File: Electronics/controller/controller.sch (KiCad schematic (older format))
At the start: 26 parts, among them P1 POWER, P2 PANEL_1, P3 PANEL_2, Q1 P55NF, SW1 SW_PUSH, U1 LM7805CT, U2 74HC595, U3 Arduino_Pro_Micro

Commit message: Moved some parts around on the board.
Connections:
- net D18: now also R2.1, SW1.1
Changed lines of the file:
@@
 EESchema Schematic File Version 2
-LIBS:cylindric
-LIBS:borniers
 LIBS:power
 LIBS:device
@@
 LIBS:contrib
 LIBS:valves
-LIBS:controller-cache
+LIBS:borniers
+LIBS:cylindric
+LIBS:digit_board-cache
 EELAYER 25 0
 EELAYER END
@@
 	1    0    0    -1
 $EndComp
-Text Label 7225 1300 0    60   ~ 0
+Text Label 7200 1300 0    60   ~ 0
 D18
 Text Notes 7200 750  0    60   ~ 0
@@
 	4100 2350 4100 2450
 Wire Wire Line
-	3900 2350 4300 2350
+	3900 2350 4100 2350
+Wire Wire Line
+	4100 2350 4300 2350
 Wire Wire Line
 	4500 1500 4550 1500
@@
 	4450 1700 4550 1700
 Wire Wire Line
-	4500 950  4500 1500
+	4500 950  4500 1100
+Wire Wire Line
+	4500 1100 4500 1500
 Wire Wire Line
 	4500 1100 4550 1100
@@
 	3900 2250 3900 2350
 Wire Wire Line
-	5700 1800 6600 1800
-Wire Wire Line
-	5700 1350 6250 1350
-Wire Wire Line
-	1450 1400 1850 1400
+	5700 1800 6000 1800
+Wire Wire Line
+	6000 1800 6600 1800
+Wire Wire Line
+	5700 1350 6000 1350
+Wire Wire Line
+	6000 1350 6250 1350
+Wire Wire Line
+	1450 1400 1650 1400
+Wire Wire Line
+	1650 1400 1850 1400
 Connection ~ 1650 1400
 Wire Wire Line
-	1650 1150 1650 1550
+	1650 1150 1650 1400
+Wire Wire Line
+	1650 1400 1650 1550
 Wire Wire Line
 	2250 2050 2250 1700
 Wire Wire Line
-	1450 2050 2825 2050
+	1450 2050 1650 2050
+Wire Wire Line
+	1650 2050 1800 2050
+Wire Wire Line
+	1800 2050 2250 2050
+Wire Wire Line
+	2250 2050 2825 2050
 Connection ~ 1800 2050
 Wire Notes Line
@@
 	10700 2800 8600 2800
 Wire Wire Line
-	5700 900  6600 900
+	5700 900  6000 900
+Wire Wire Line
+	6000 900  6600 900
 Wire Wire Line
 	5700 1350 5700 1400
@@
 	4300 1350 4300 1300
 Wire Wire Line
-	4300 1300 4550 1300
+	4300 1300 4450 1300
+Wire Wire Line
+	4450 1300 4550 1300
 Wire Wire Line
 	3900 1750 3900 1600
 Wire Wire Line
-	3750 1600 4000 1600
+	3750 1600 3900 1600
+Wire Wire Line
+	3900 1600 4000 1600
 Wire Wire Line
 	3200 3250 3400 3250
@@
 	1350 5350 1350 5100
 Wire Bus Line
-	3500 4525 6150 4525
+	3500 4375 6150 4375
 Entry Wire Line
 	3400 3250 3500 3350
@@
 	3400 3950 3500 4050
 Wire Bus Line
-	3500 3175 3500 4525
+	3500 3175 3500 3350
+Wire Bus Line
+	3500 3350 3500 3450
+Wire Bus Line
+	3500 3450 3500 3550
+Wire Bus Line
+	3500 3550 3500 3650
+Wire Bus Line
+	3500 3650 3500 3750
+Wire Bus Line
+	3500 3750 3500 3850
+Wire Bus Line
+	3500 3850 3500 3950
+Wire Bus Line
+	3500 3950 3500 3900
+Wire Bus Line
+	3500 3900 3500 4375
 Entry Wire Line
 	6050 4850 6150 4750
@@
 	6050 5550 6150 5450
 Wire Bus Line
-	6150 4525 6150 5600
+	6150 4375 6150 4600
+Wire Bus Line
+	6150 4600 6150 4750
+Wire Bus Line
+	6150 4750 6150 4850
+Wire Bus Line
+	6150 4850 6150 4950
+Wire Bus Line
+	6150 4950 6150 5050
+Wire Bus Line
+	6150 5050 6150 5150
+Wire Bus Line
+	6150 5150 6150 5250
+Wire Bus Line
+	6150 5250 6150 5350
+Wire Bus Line
+	6150 5350 6150 5450
+Wire Bus Line
+	6150 5450 6150 5600
 Wire Wire Line
 	9050 2050 8900 2050
@@
 $EndComp
 Wire Wire Line
-	2825 1150 2825 1550
+	2825 1150 2825 1400
+Wire Wire Line
+	2825 1400 2825 1550
 Connection ~ 2825 1400
 Wire Wire Line
@@
 $EndComp
 Wire Wire Line
-	7400 1150 7400 1450
+	7400 1150 7400 1300
+Wire Wire Line
+	7400 1300 7400 1450
 Wire Wire Line
 	7400 1450 7500 1450
@@
 $EndComp
 Wire Wire Line
-	7400 1300 7250 1300
+	7400 1300 7200 1300
 Connection ~ 7400 1300
 $EndSCHEMATC

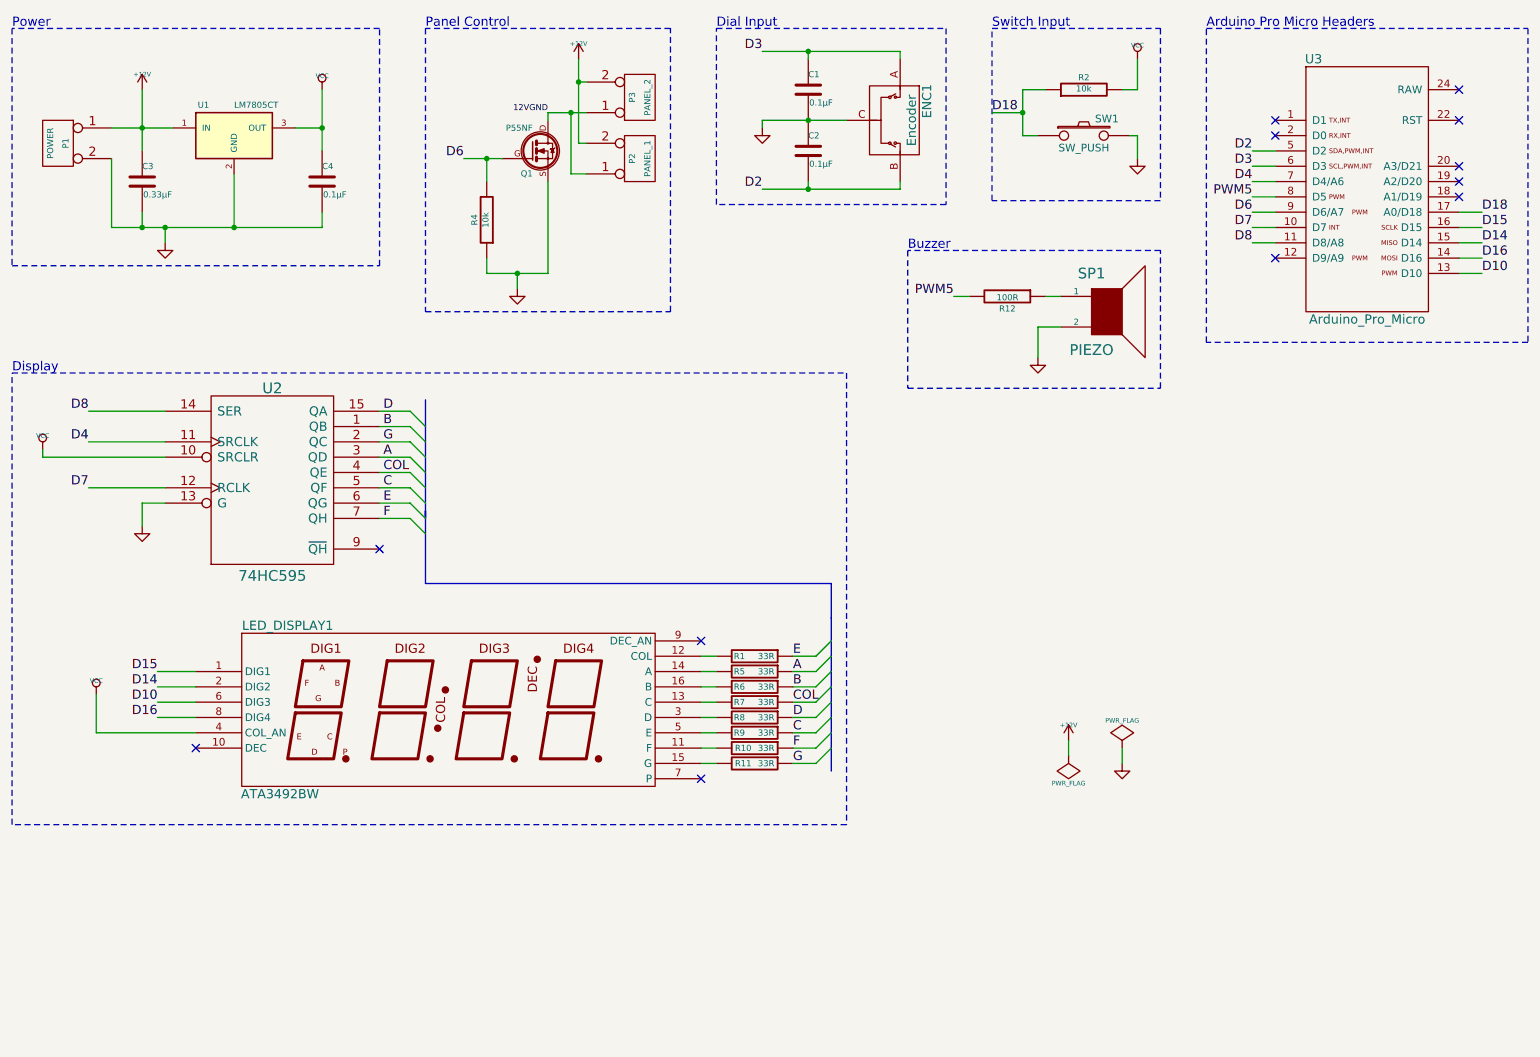
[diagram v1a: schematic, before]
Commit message: Tidied up some visual layout issues.
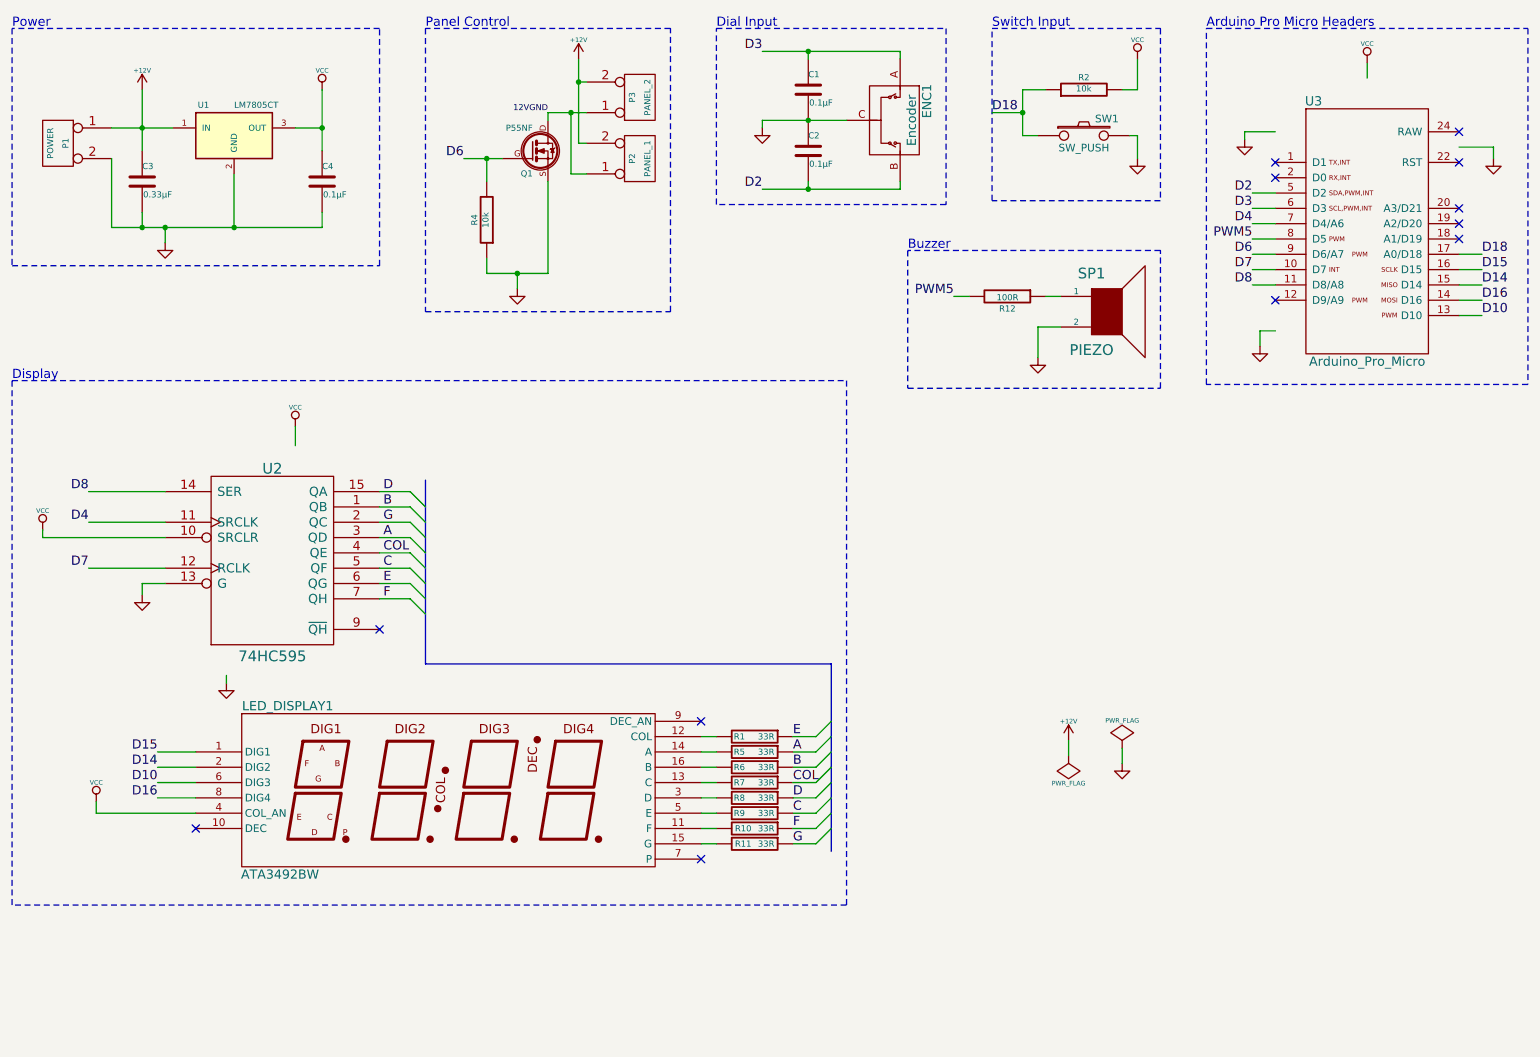
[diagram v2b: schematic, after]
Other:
- moved on the sheet: LED_DISPLAY1, R1, R10, R11, R5, R6, R7, R8, R9, U2, U3

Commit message: Changes for v1.1
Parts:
- R12: value 100R -> 120R
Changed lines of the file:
@@
 LIBS:contrib
 LIBS:valves
+LIBS:controller-cache
 EELAYER 25 0
 EELAYER END
@@
 P 7300 2500
 F 0 "R12" V 7380 2500 40  0000 C CNN
-F 1 "100R" V 7307 2501 40  0000 C CNN
+F 1 "120R" V 7307 2501 40  0000 C CNN
 F 2 "Discret:R3" V 7230 2500 30  0001 C CNN
 F 3 "~" H 7300 2500 30  0000 C CNN
